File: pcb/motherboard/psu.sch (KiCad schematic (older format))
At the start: 23 parts, among them J11 103741-1, J12 103741-1, J16 103741-1, J9 103777-5, U3 ADP2302ARDZ-5.0, U4 ADP2303ARDZ-3.3

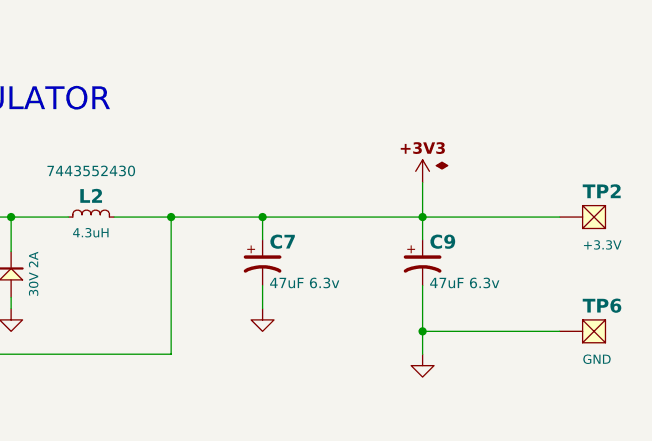
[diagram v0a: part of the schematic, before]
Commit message: Fixed wrong cap value for C24 and part # for C7,C9
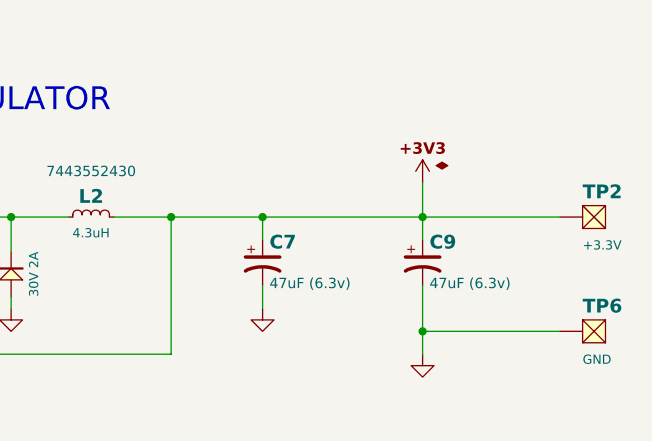
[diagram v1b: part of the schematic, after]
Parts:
- C7: value 47uF 6.3v -> 47uF (6.3v)
- C9: value 47uF 6.3v -> 47uF (6.3v); Part (none) -> GRM31CR60J476ME19K; Part# GRM31CR60J476ME19K -> (none)
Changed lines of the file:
@@
 P 8500 5300
 F 0 "C7" H 8530 5390 60  0000 L CNB
-F 1 "47uF 6.3v" H 8530 5210 45  0000 L CNN
+F 1 "47uF (6.3v)" H 8530 5210 45  0000 L CNN
 F 2 "SMT:CPL-1206" H 8535 5145 40  0001 L CNN
 F 3 "" H 8500 5400 60  0000 C CNN
@@
 P 9200 5300
 F 0 "C9" H 9230 5390 60  0000 L CNB
-F 1 "47uF 6.3v" H 9230 5210 45  0000 L CNN
+F 1 "47uF (6.3v)" H 9230 5210 45  0000 L CNN
 F 2 "SMT:CPL-1206" H 9235 5145 40  0001 L CNN
 F 3 "" H 9200 5400 60  0000 C CNN
-F 4 "GRM31CR60J476ME19K" H 9235 5465 45  0001 L CNN "Part#"
+F 4 "GRM31CR60J476ME19K" H 9235 5465 45  0001 L CNN "Part"
 F 5 "Murata" H 9200 5300 60  0001 C CNN "MFG"
 F 6 "Passive" H 9200 5300 60  0001 C CNN "Family"
